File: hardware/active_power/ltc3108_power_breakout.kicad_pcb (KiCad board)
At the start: 2 copper layers, 77 x 57 mm, 13 parts, among them J1 TEG, J2 External_LPR6235_752SML, J3 OUT_3V3_LAB, J4 EXTERNAL_VSTORE_SUPERCAP_6V3, J5 PGOOD_MONITOR, U1 LTC3108EGN

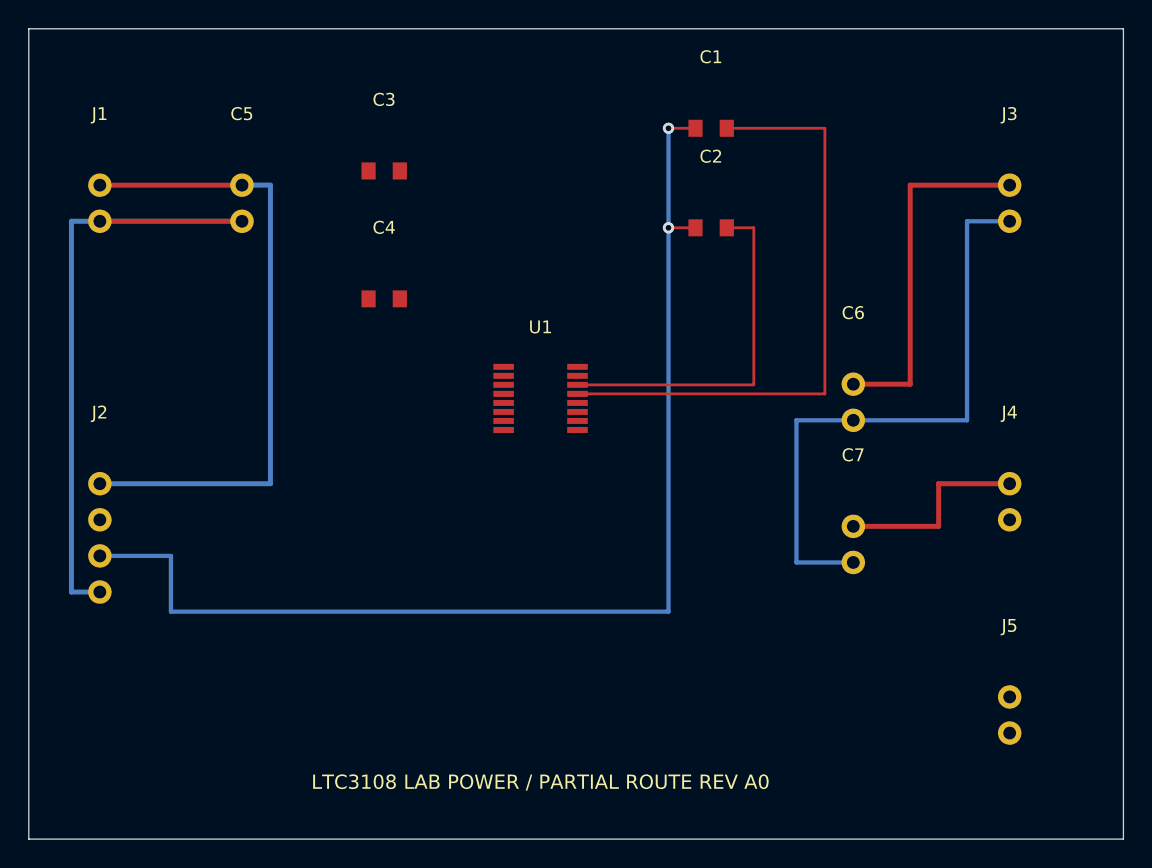
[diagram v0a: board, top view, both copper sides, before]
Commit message: hardware: join LTC3108 transformer secondary to C1/C2 over isolated B.Cu and plated vias
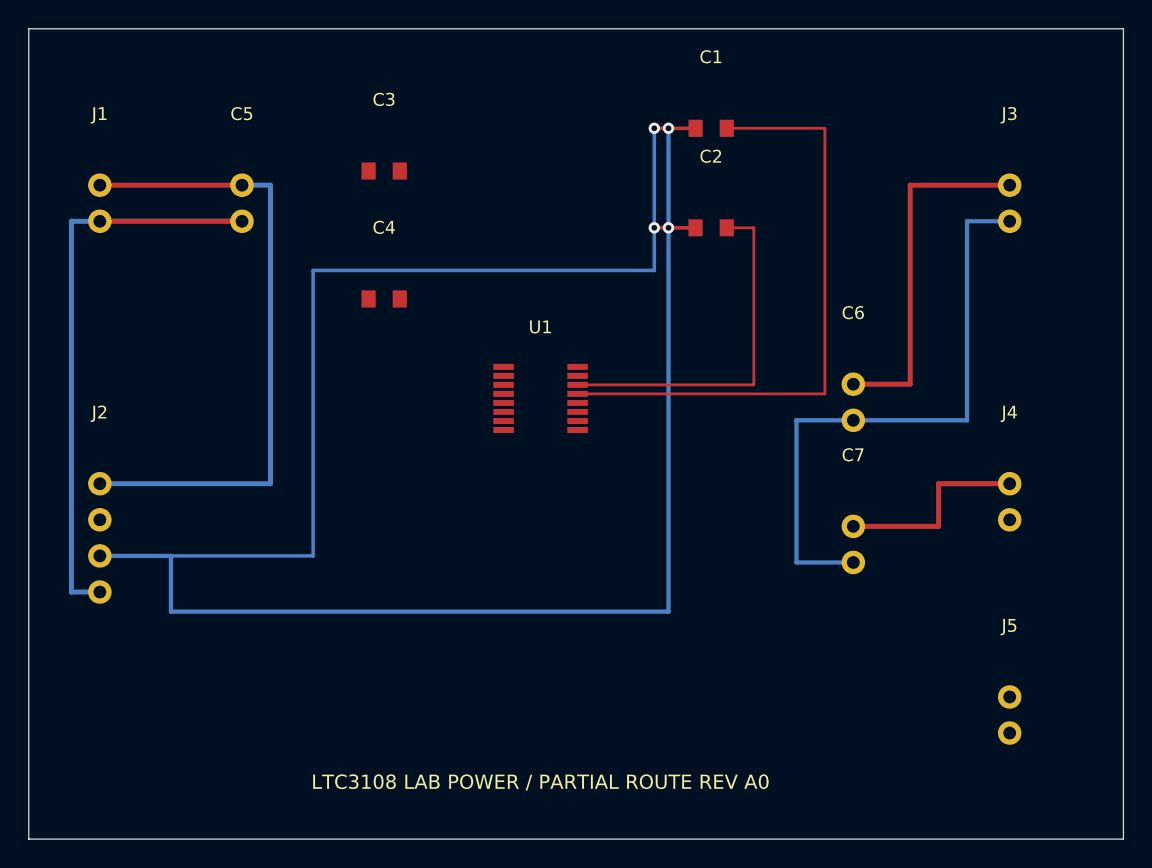
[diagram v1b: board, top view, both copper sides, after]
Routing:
- net SEC_HI: track 81.7 -> 156.6 mm, vias 2 -> 4
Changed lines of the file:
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@@
 (via (at 55 17) (size 0.8) (drill 0.4) (layers "F.Cu" "B.Cu") (net 12))
 (via (at 55 24) (size 0.8) (drill 0.4) (layers "F.Cu" "B.Cu") (net 12))
+(segment (start 56.9 17) (end 54 17) (width 0.25) (layer "F.Cu") (net 12))
+(segment (start 56.9 24) (end 54 24) (width 0.25) (layer "F.Cu") (net 12))
+(segment (start 54 17) (end 54 24) (width 0.25) (layer "B.Cu") (net 12))
+(segment (start 15 47.08) (end 30 47.08) (width 0.25) (layer "B.Cu") (net 12))
+(segment (start 30 47.08) (end 30 27) (width 0.25) (layer "B.Cu") (net 12))
+(segment (start 30 27) (end 54 27) (width 0.25) (layer "B.Cu") (net 12))
+(segment (start 54 27) (end 54 24) (width 0.25) (layer "B.Cu") (net 12))
+(via (at 54 17) (size 0.8) (drill 0.4) (layers "F.Cu" "B.Cu") (net 12))
+(via (at 54 24) (size 0.8) (drill 0.4) (layers "F.Cu" "B.Cu") (net 12))
 (gr_line (start 10 10) (end 87 10) (stroke (width 0.05) (type default)) (layer "Edge.Cuts"))
 (gr_line (start 87 10) (end 87 67) (stroke (width 0.05) (type default)) (layer "Edge.Cuts"))

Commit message: fix(cad): remove duplicate secondary traces and vias after concurrent reference-route integration
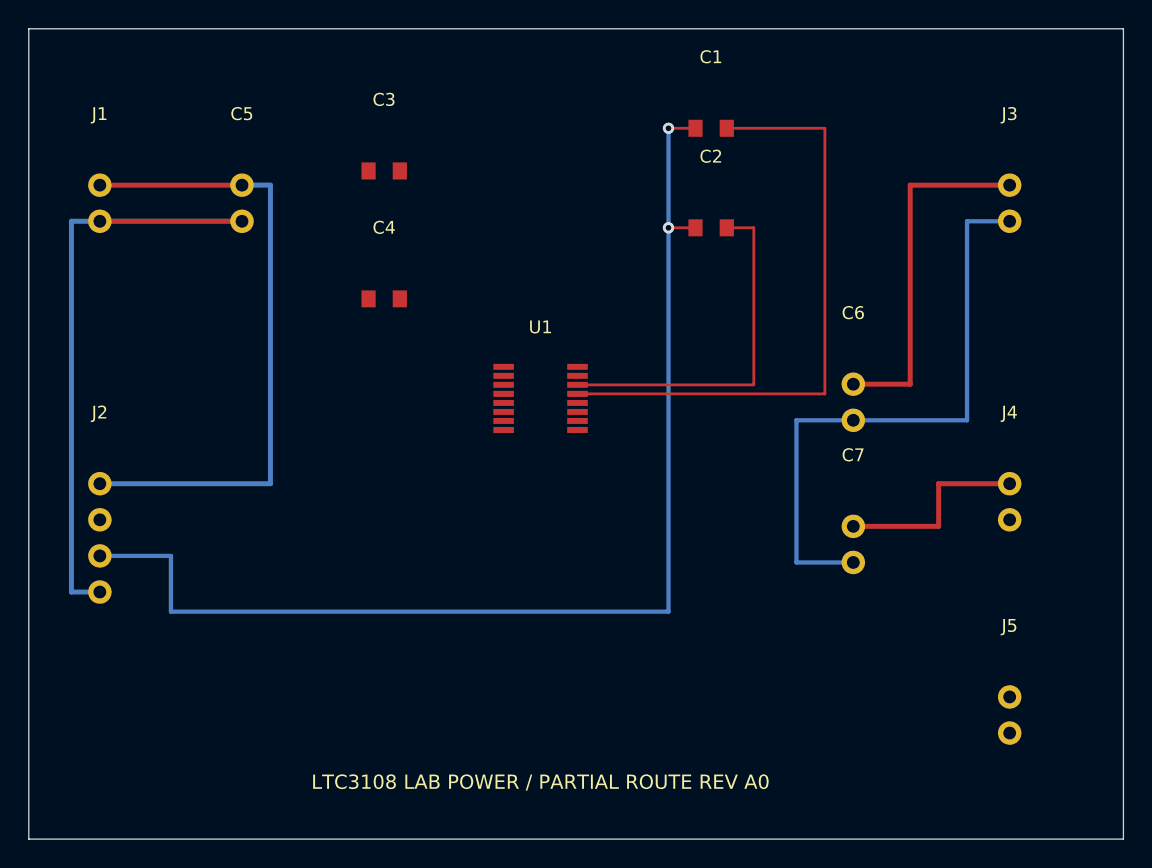
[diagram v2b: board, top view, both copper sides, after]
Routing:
- net SEC_HI: track 156.6 -> 81.7 mm, vias 4 -> 2
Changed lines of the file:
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@@
 (via (at 55 17) (size 0.8) (drill 0.4) (layers "F.Cu" "B.Cu") (net 12))
 (via (at 55 24) (size 0.8) (drill 0.4) (layers "F.Cu" "B.Cu") (net 12))
-(segment (start 56.9 17) (end 54 17) (width 0.25) (layer "F.Cu") (net 12))
-(segment (start 56.9 24) (end 54 24) (width 0.25) (layer "F.Cu") (net 12))
-(segment (start 54 17) (end 54 24) (width 0.25) (layer "B.Cu") (net 12))
-(segment (start 15 47.08) (end 30 47.08) (width 0.25) (layer "B.Cu") (net 12))
-(segment (start 30 47.08) (end 30 27) (width 0.25) (layer "B.Cu") (net 12))
-(segment (start 30 27) (end 54 27) (width 0.25) (layer "B.Cu") (net 12))
-(segment (start 54 27) (end 54 24) (width 0.25) (layer "B.Cu") (net 12))
-(via (at 54 17) (size 0.8) (drill 0.4) (layers "F.Cu" "B.Cu") (net 12))
-(via (at 54 24) (size 0.8) (drill 0.4) (layers "F.Cu" "B.Cu") (net 12))
 (gr_line (start 10 10) (end 87 10) (stroke (width 0.05) (type default)) (layer "Edge.Cuts"))
 (gr_line (start 87 10) (end 87 67) (stroke (width 0.05) (type default)) (layer "Edge.Cuts"))
